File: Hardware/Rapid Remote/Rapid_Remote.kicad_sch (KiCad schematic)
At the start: 44 parts, among them J1 Conn_01x02_Socket, U1 MIC5504-3.3YM5, U3 WS4518D, U4 XB6096I2SV, U5 ESP32-C3-MINI-1

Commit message: updated to use mounting holes as jig for stencil
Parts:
- R6: value 47.5k -> 5k
- s1: footprint rapidtraining:TS-1177-C-B-B -> Personal:TS-1177-C-B-B
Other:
- note added: "5k for 400mA 7.5k for 250mA"
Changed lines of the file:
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@@
     (stroke (width 0) (type default))
+  )
+  (text "5k for 400mA\n7.5k for 250mA" (at 77.47 99.06 0)
+    (effects (font (size 1.27 1.27)) (justify left bottom))
   )
   (global_label "USB_D+" (shape input) (at 31.75 154.94 0) (fields_autoplaced)
@@
       (effects (font (size 1.778 1.5113)) (justify left bottom))
     )
-    (property "Value" "47.5k" (at 69.088 93.98 0)
+    (property "Value" "5k" (at 69.088 93.98 0)
       (effects (font (size 1.778 1.5113)) (justify left bottom))
     )
@@
     )
   )
-  (symbol (lib_name "BUTTON_4PIN_TS_1177_2") (lib_id "personal2:BUTTON_4PIN_TS_1177") (at 198.12 41.91 0) (unit 1)
+  (symbol (lib_id "personal2:BUTTON_4PIN_TS_1177") (at 198.12 41.91 0) (unit 1)
     (in_bom yes) (on_board yes) (dnp no)
     (property "Reference" "s1" (at 198.12 33.02 0)
@@
       (effects (font (size 1.27 1.27)) hide)
     )
-    (property "Footprint" "rapidtraining:TS-1177-C-B-B" (at 198.12 41.91 0)
-      (effects (font (size 1.27 1.27)) hide)
-    )
+    (property "Footprint" "Personal:TS-1177-C-B-B" (at 198.12 41.91 0)
+      (effects (font (size 1.27 1.27)) hide)
+    )

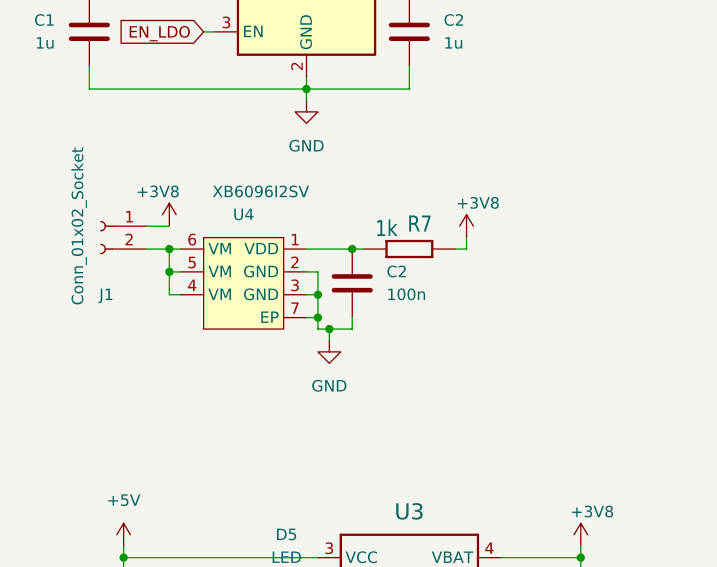
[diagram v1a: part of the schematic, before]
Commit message: Updated Footprints for LED
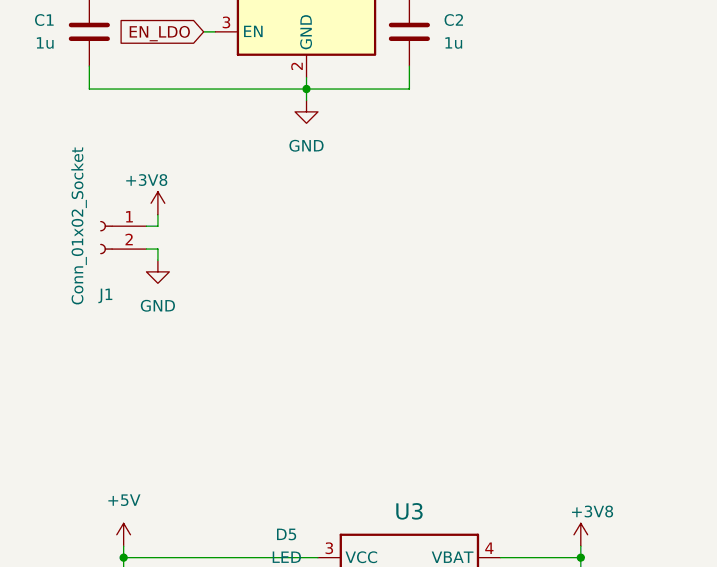
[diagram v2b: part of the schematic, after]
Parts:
- removed C2: 100n, Capacitor_SMD:C_0603_1608Metric, symbol Device:C
- removed R7: 1k, Resistor_SMD:R_0603_1608Metric, symbol picoclick_c3_v1.1-eagle-import:moekoe_rcl_R0402
- removed U4: XB6096I2SV, Package_DFN_QFN:DFN-6-1EP_2x2mm_P0.65mm_EP1x1.6mm, symbol personal2:XB6096I2SV_
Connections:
- net GND: now also J1.2 (Pin_2)
